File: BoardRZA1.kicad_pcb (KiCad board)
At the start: 4 copper layers, 99.9 x 80 mm, 137 parts, among them CON1 USB-MINI-B, CON2 USB-MINI-B, CON3 con-microSD, CON4 BARREL_JACK, J1 HR911105A, P1 CONN_5X2, SW1 RESET, U1 RZ-A1L, U2 OSC_4PIN, U3 OSC_4PIN, U4 N25QXXX, U5 AS4C16M16S, U6 BA3259HFP, U7 BU42xx, U8 KSZ8041MLL, X1 32.768k, X2 20MHz

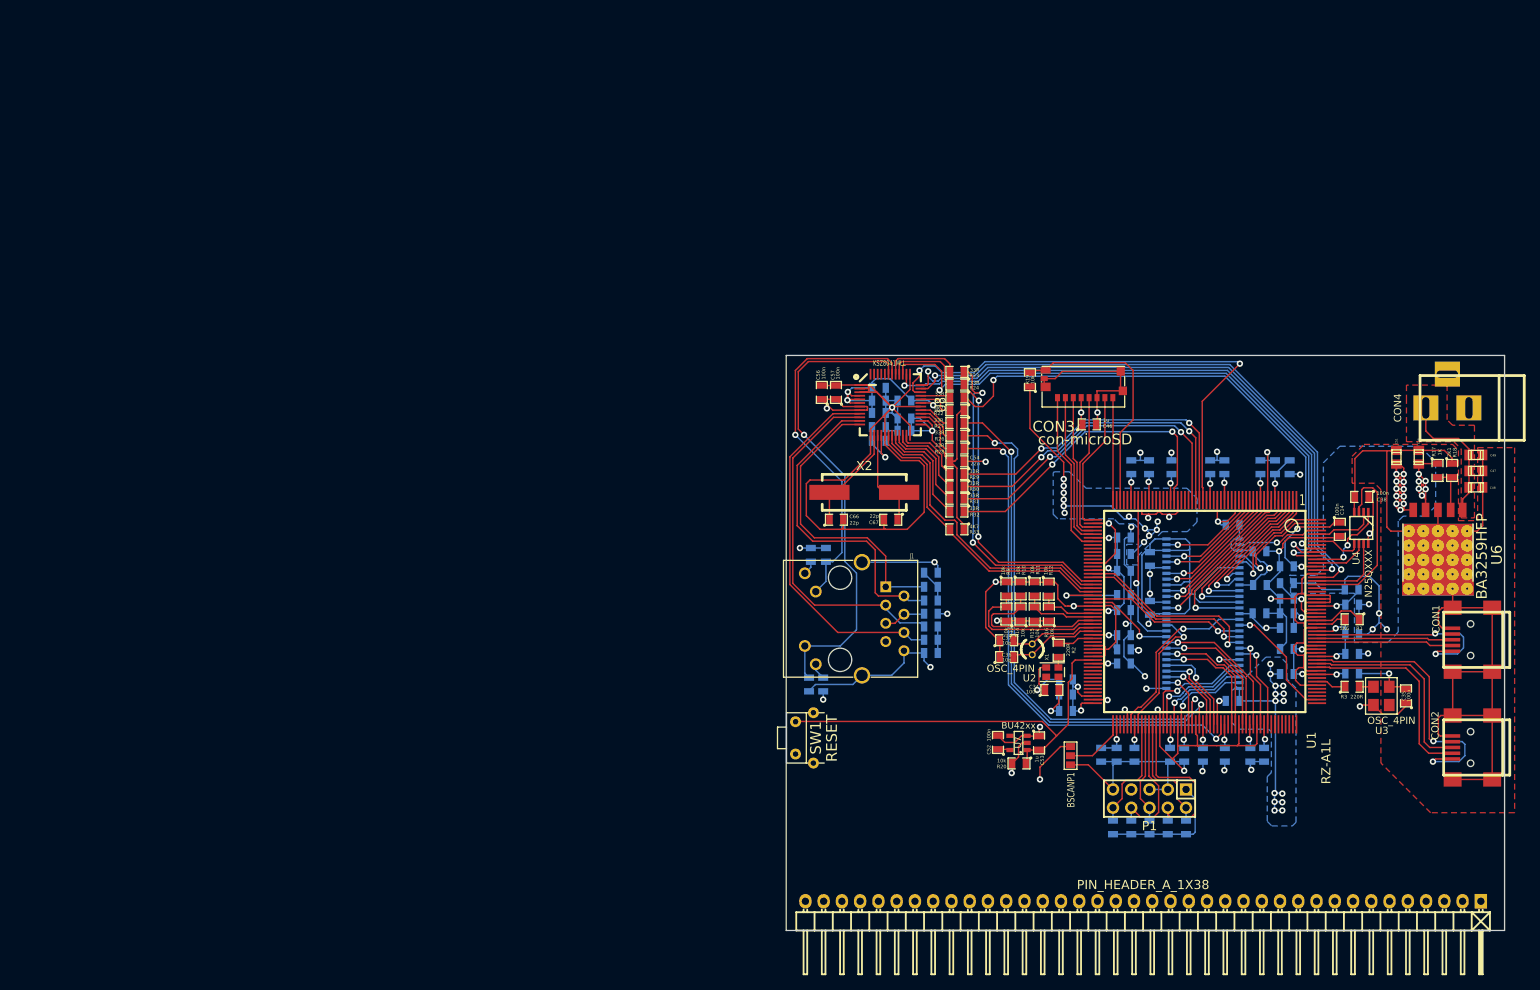
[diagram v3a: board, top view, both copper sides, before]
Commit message: GPIO routed
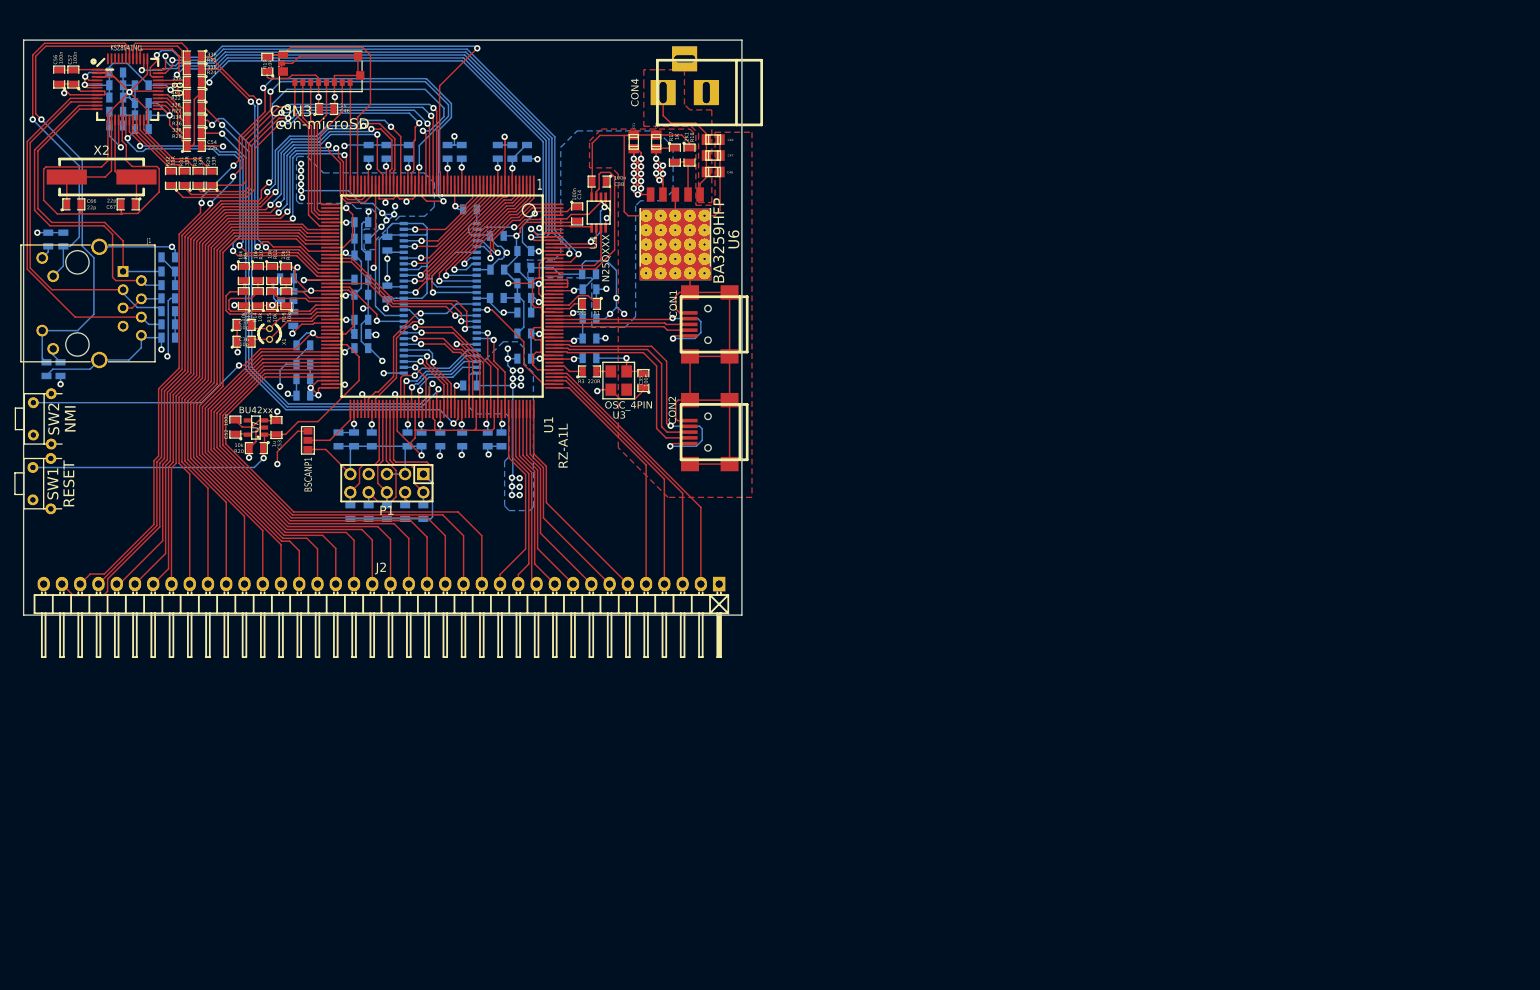
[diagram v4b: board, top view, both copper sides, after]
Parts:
- removed PIN_HEADER_A_1X38: Val**, Pin_Headers:Pin_Header_Angled_1x38
- added J2: SIL38, Pin_Headers:Pin_Header_Angled_1x38, F.Cu at (69.7, 93.3)
- added R42: 10k, SMD_Packages:SM0805, B.Cu at (58.8, 60.1)
- added SW2: NMI, PushButton:RigthAnglePush, F.Cu at (22.5, 70.3)
- C34, R2, R33, U2: moved to B.Cu
- moved R33 126.3 mm to (36.3, 30.0)
- moved C34 120.9 mm to (56.5, 50.7)
- moved R32 118.8 mm to (40.4, 36.8), turned to 90 degrees
- moved U2 118.6 mm to (56.6, 53.2)
- moved R31 116.3 mm to (42.3, 36.8), turned to 90 degrees
- moved R2 116.0 mm to (57.4, 56.4), turned to 90 degrees
- moved C27 114.8 mm to (68.3, 73.2)
- moved C36 114.8 mm to (50.5, 59.6)
- moved C37 114.8 mm to (50.5, 57.2)
- moved C53 114.8 mm to (55.1, 71.5)
- moved C56 114.8 mm to (24.8, 22.7)
- moved C58 114.8 mm to (32.8, 27.6)
- moved C60 114.8 mm to (32.8, 22.1)
- moved C61 114.8 mm to (32.8, 23.9)
- moved C63 114.8 mm to (32.8, 25.6)
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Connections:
- net Net-(U1-Pad37) renamed /P8_11
- U1 pad 100: Net-(U1-Pad100) -> /P1_14
- U1 pad 101: Net-(U1-Pad101) -> /P1_15
- U1 pad 149: Net-(U1-Pad149) -> /P1_0
- U1 pad 150: Net-(U1-Pad150) -> /P1_1
- U1 pad 151: Net-(U1-Pad151) -> /P1_2
- U1 pad 152: Net-(U1-Pad152) -> /P1_3
- U1 pad 153: Net-(U1-Pad153) -> /P1_4
- U1 pad 154: Net-(U1-Pad154) -> /P1_5
- U1 pad 155: Net-(U1-Pad155) -> /P1_6
- U1 pad 156: Net-(U1-Pad156) -> /P1_7
- U1 pad 157: Net-(U1-Pad157) -> /P3_15
- U1 pad 159: Net-(U1-Pad159) -> /P2_7
- U1 pad 160: Net-(U1-Pad160) -> /P2_8
- U1 pad 161: Net-(U1-Pad161) -> /P2_9
- U1 pad 31: Net-(U1-Pad31) -> /P6_6
- U1 pad 32: Net-(U1-Pad32) -> /P6_7
- U1 pad 33: Net-(U1-Pad33) -> /P6_8
- U1 pad 38: Net-(U1-Pad38) -> /P6_9
- U1 pad 40: Net-(U1-Pad40) -> /P6_10
- U1 pad 41: Net-(U1-Pad41) -> /P6_11
- U1 pad 43: Net-(U1-Pad43) -> /P6_12
- U1 pad 46: Net-(U1-Pad46) -> /P6_13
- U1 pad 48: Net-(U1-Pad48) -> /P6_14
- U1 pad 49: Net-(U1-Pad49) -> /P6_15
- U1 pad 60: Net-(U1-Pad60) -> /P7_8
- U1 pad 61: Net-(U1-Pad61) -> /P7_9
- U1 pad 62: Net-(U1-Pad62) -> /P7_10
- U1 pad 63: Net-(U1-Pad63) -> /P7_11
- U1 pad 64: Net-(U1-Pad64) -> /P7_12
- U1 pad 66: Net-(U1-Pad66) -> /P7_13
- U1 pad 94: Net-(U1-Pad94) -> /P1_8
- U1 pad 95: Net-(U1-Pad95) -> /P1_9
- U1 pad 96: Net-(U1-Pad96) -> /P1_10
- U1 pad 97: Net-(U1-Pad97) -> /P1_11
- U1 pad 98: Net-(U1-Pad98) -> /P1_12
- U1 pad 99: Net-(U1-Pad99) -> /P1_13
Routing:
- net /P6_7: track 0.00 -> 128.6 mm, vias 0 -> 4
- net /P6_6: track 0.00 -> 126.0 mm, vias 0 -> 2
- net /P6_8: track 0.00 -> 117.9 mm, vias 0 -> 4
- net /P6_9: track 0.00 -> 99.6 mm, vias 0 -> 2
- net /P6_10: track 0.00 -> 96.7 mm, vias 0 -> 2
- net /P6_11: track 0.00 -> 94.5 mm, vias 0 -> 2
- net /P6_12: track 0.00 -> 91.4 mm, vias 0 -> 2
- net /P6_13: track 0.00 -> 91.3 mm, vias 0 -> 2
- net /P6_14: track 0.00 -> 90.4 mm, vias 0 -> 2
- net /P6_15: track 0.00 -> 89.7 mm, vias 0 -> 2
- net /P7_13: track 0.00 -> 74.6 mm
- net /P7_12: track 0.00 -> 72.9 mm
- net /P7_11: track 0.00 -> 71.4 mm
- net /P7_10: track 0.00 -> 70.5 mm
- net /P7_9: track 0.00 -> 70.2 mm
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
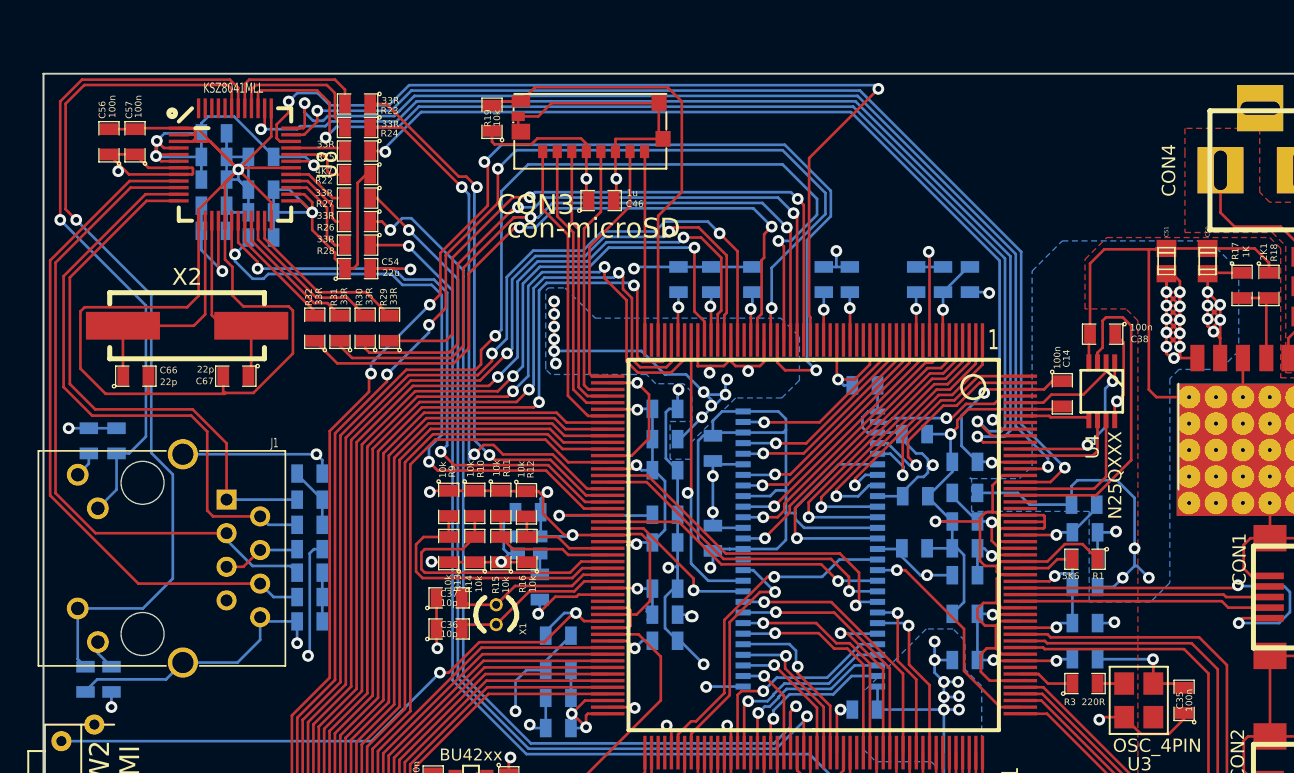
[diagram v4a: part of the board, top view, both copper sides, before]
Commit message: Leds&buttons rerout eth out
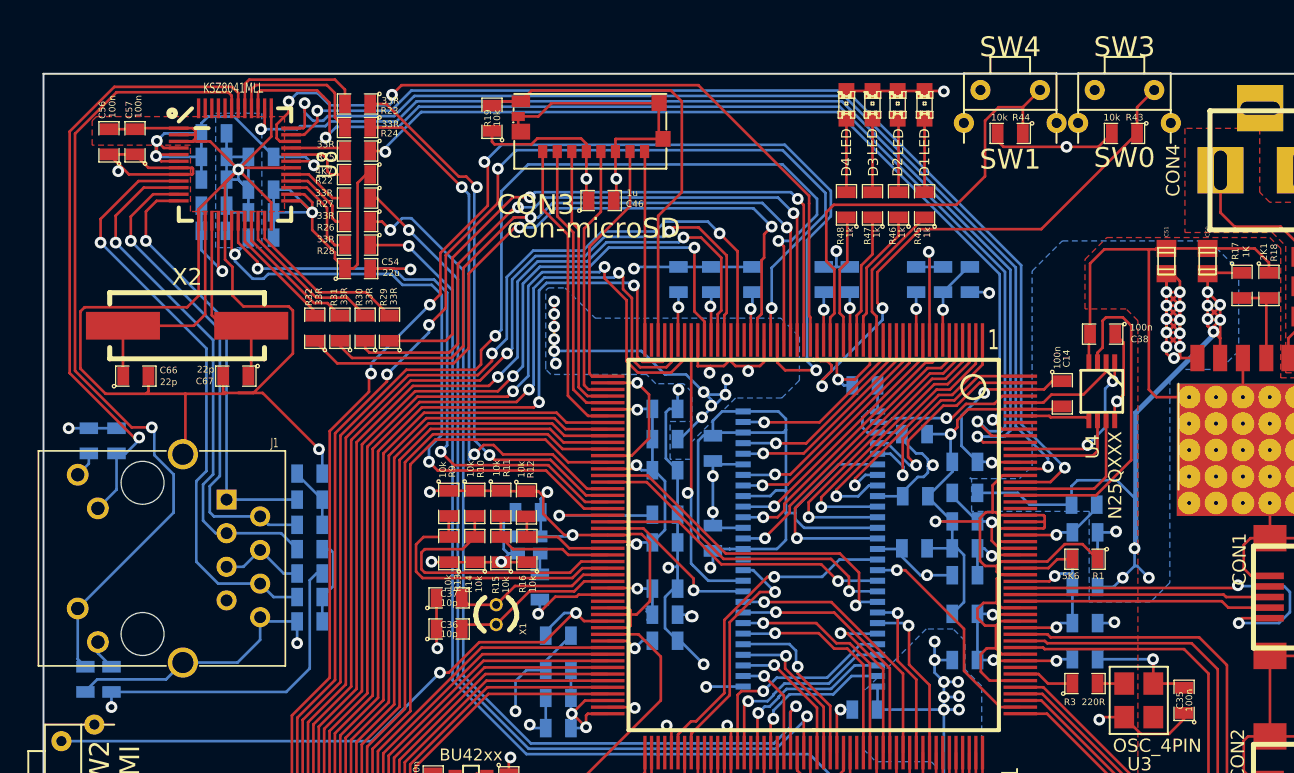
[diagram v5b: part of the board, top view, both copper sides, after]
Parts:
- added D1: LED, LEDs:LED-0805, F.Cu at (86.5, 19.9)
- added D2: LED, LEDs:LED-0805, F.Cu at (84.5, 19.9)
- added D3: LED, LEDs:LED-0805, F.Cu at (82.5, 19.9)
- added D4: LED, LEDs:LED-0805, F.Cu at (80.6, 19.9)
- added R43: 10k, SMD_Packages:SM0805, F.Cu at (101.6, 22.1)
- added R44: 10k, SMD_Packages:SM0805, F.Cu at (93.0, 22.1)
- added R45: 1k, SMD_Packages:SM0805, F.Cu at (86.5, 27.5)
- added R46: 1k, SMD_Packages:SM0805, F.Cu at (84.5, 27.5)
- added R47: 1k, SMD_Packages:SM0805, F.Cu at (82.5, 27.5)
- added R48: 1k, SMD_Packages:SM0805, F.Cu at (80.6, 27.5)
- added SW3: SW0, PushButton:RigthAnglePush, F.Cu at (101.6, 20.1)
- added SW4: SW1, PushButton:RigthAnglePush, F.Cu at (93.0, 20.1)
- moved L10 1.84 mm to (40.0, 55.4)
- moved R40 1.78 mm to (40.0, 53.5)
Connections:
- J1 pad 10: /LED0 -> /ET_LED0
- J1 pad 11: /LED1 -> /ET_LED1
- R34 pad 1: /LED0 -> /ET_LED0
- R35 pad 2: /LED1 -> /ET_LED1
- U1 pad 17: Net-(U1-Pad17) -> /LED0
- U1 pad 19: Net-(U1-Pad19) -> /LED1
- U1 pad 20: Net-(U1-Pad20) -> /LED2
- U1 pad 22: Net-(U1-Pad22) -> /LED3
- U1 pad 24: Net-(U1-Pad24) -> /SW1
- U1 pad 26: Net-(U1-Pad26) -> /SW0
- U8 pad 42: /LED0 -> /ET_LED0
- U8 pad 43: /LED1 -> /ET_LED1
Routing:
- net /ET_LED1: track 0.00 -> 61.8 mm, vias 0 -> 1
- net /LED1: track 66.8 -> 10.4 mm, vias 1 -> 0
- net /ET_LED0: track 0.00 -> 48.2 mm, vias 0 -> 1
- net /SW0: track 0.00 -> 43.0 mm, vias 0 -> 2
- net /LED0: track 51.4 -> 11.1 mm, vias 1 -> 0
- net +1.2V: track 49.2 -> 86.9 mm
- net /SW1: track 0.00 -> 34.5 mm
- net +3.3V: track 275.1 -> 306.9 mm, vias 53 -> 54
- net /ET_TXEN: track 71.5 -> 59.7 mm
- net /LED2: track 0.00 -> 9.77 mm
- net /LED3: track 0.00 -> 9.65 mm
- net Net-(J1-Pad3): track 50.1 -> 40.6 mm, vias 0 -> 1
- net Net-(J1-Pad1): track 42.0 -> 32.5 mm, vias 0 -> 1
- net Net-(J1-Pad2): track 45.1 -> 36.8 mm, vias 0 -> 1
- net Net-(J1-Pad6): track 51.8 -> 45.4 mm, vias 0 -> 1
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- added copper zone on B.Cu, net VSS

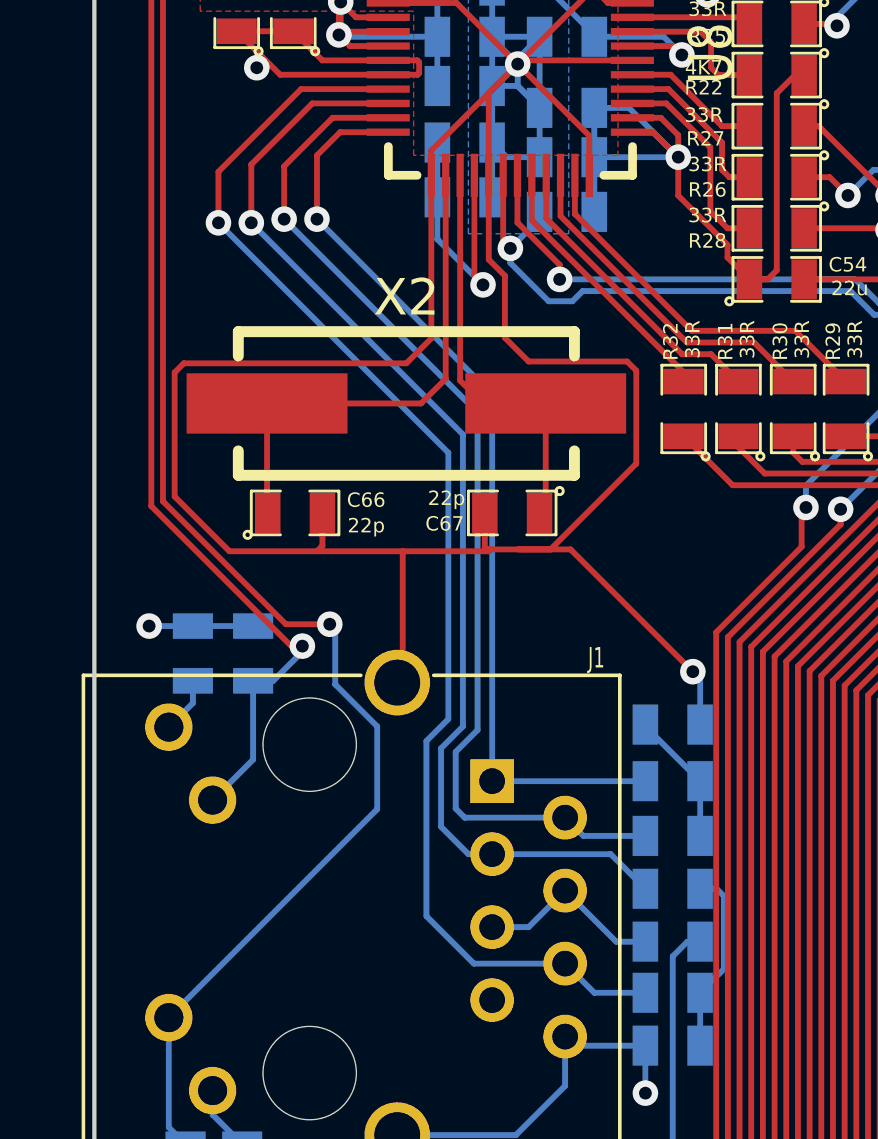
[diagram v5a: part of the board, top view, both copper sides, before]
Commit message: Cambia XTAL 25MHz Phy por OSC 25MHz
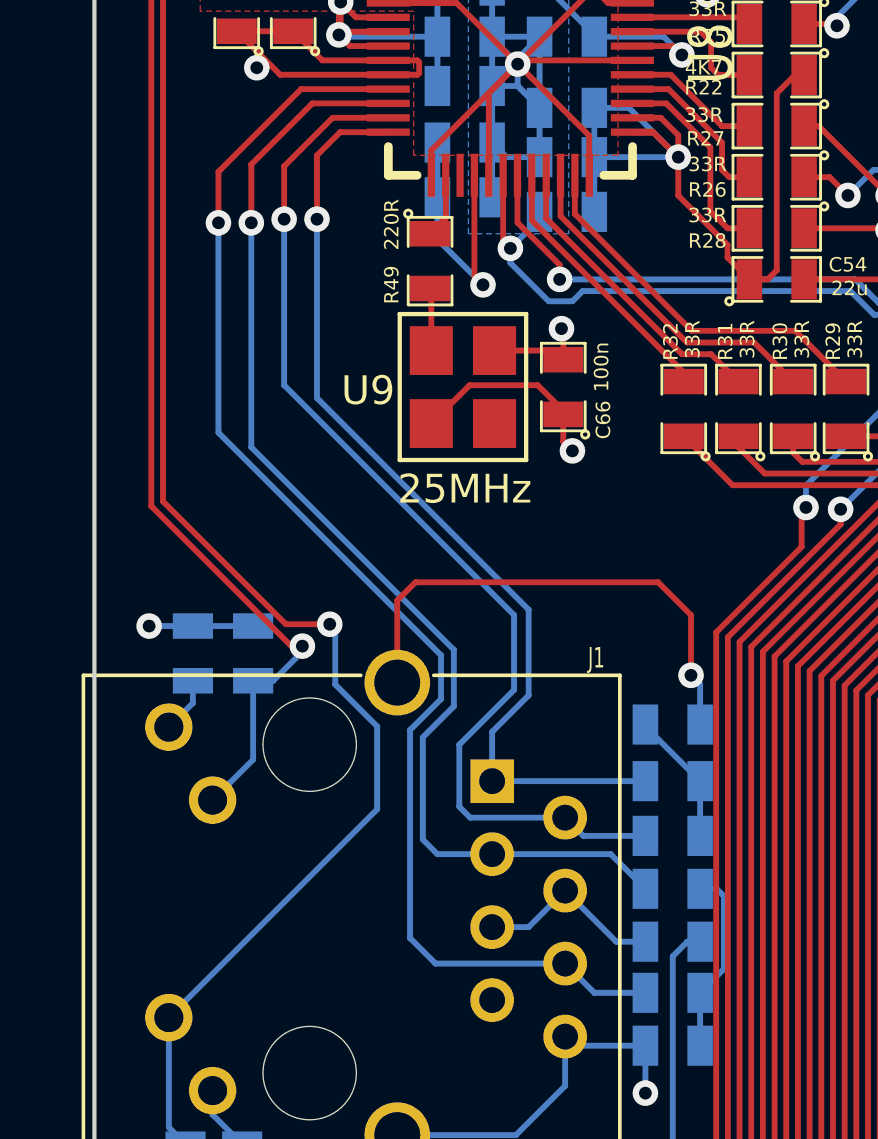
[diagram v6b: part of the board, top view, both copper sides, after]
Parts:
- removed C67: 22p, SMD_Packages:SM0805
- removed X2: 20MHz, Crystals:Crystal_HC49-SD_SMD
- added R49: 220R, SMD_Packages:SM0805, F.Cu at (31.6, 31.7)
- added U9: 25MHz, OSC_4PIN:OSC_4PIN, F.Cu at (32.7, 36.1)
- C66: value 22p -> 100n
- moved C66 10.3 mm to (36.2, 36.1), turned to 90 degrees
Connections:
- C66 pad 1: Net-(C66-Pad1) -> +3.3V
- U8 pad 14: Net-(C66-Pad1) -> /ETH_CLK
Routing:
- net VSS: track 677.2 -> 629.8 mm, vias 36 -> 37
- net Net-(C66-Pad1): track 17.5 -> 0.00 mm
- net Net-(U8-Pad15): track 14.4 -> 0.00 mm
- net +3.3V: track 306.9 -> 313.9 mm, vias 54 -> 55
- net /ETH_CLK: track 0.00 -> 2.26 mm
- net Net-(R49-Pad2): track 0.00 -> 2.18 mm
- net Net-(J1-Pad1): track 32.5 -> 33.5 mm
- net Net-(J1-Pad6): track 45.4 -> 46.4 mm
- net Net-(J1-Pad3): track 40.6 -> 41.5 mm
- net Net-(J1-Pad2): track 36.8 -> 37.6 mm
